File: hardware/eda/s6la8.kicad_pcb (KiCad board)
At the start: 4 copper layers, 100 x 64 mm, 155 parts, among them J1 2.54mm 6 x 1 THT Vertical Male, J2 2.54mm 2 x 1 THT Vertical Male, J3 2.54mm 10 x 2 THT Horizontal 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, J4 USB4105-GF-A, J5 2.54mm 3 x 1 THT Vertical Male, U1 24LC128-I/SN, U10 XC6SLX9-2TQG144C, U11 CY7C68013A-56PVXC, U12 TLV62569DBVR, U13 TLV62569DBVR, U14 MT48LC16M16A2P-6A, U2 USBLC6-2SC6, U3 USBLC6-2SC6, U4 USBLC6-2SC6, U5 USBLC6-2SC6, U6 USBLC6-2SC6, U7 SN74LVC245APWR, U8 SN74LVC8T245PWR, U9 SN74LVC2T45DCUR, Y1 ASE-50.000MHZ-LC-T, Y2 24MHz 12pF

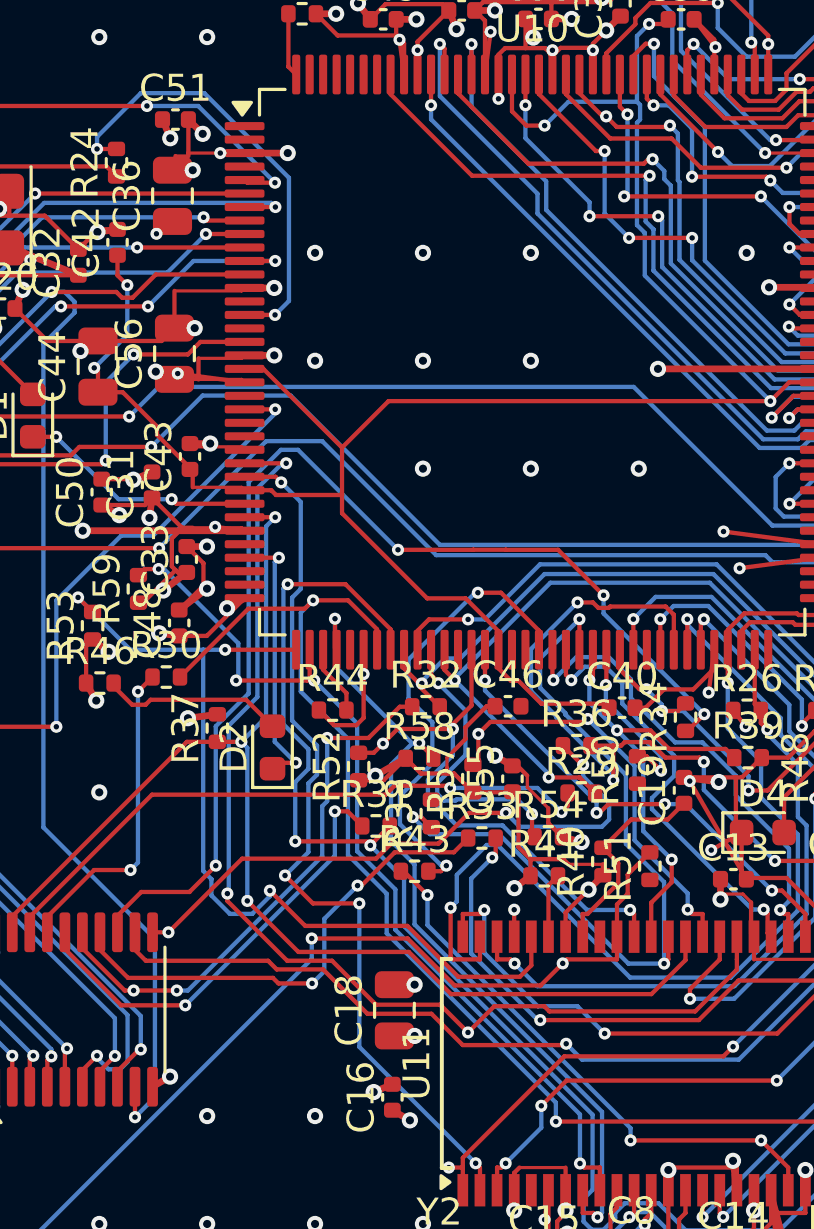
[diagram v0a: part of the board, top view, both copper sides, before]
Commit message: Add a grid router for leftover connections; 14 remain open
It closed INIT_B and two plane pads. The rest are FPGA bottom-row pads
enclosed by neighbouring escape routes and need tracks moved by hand.
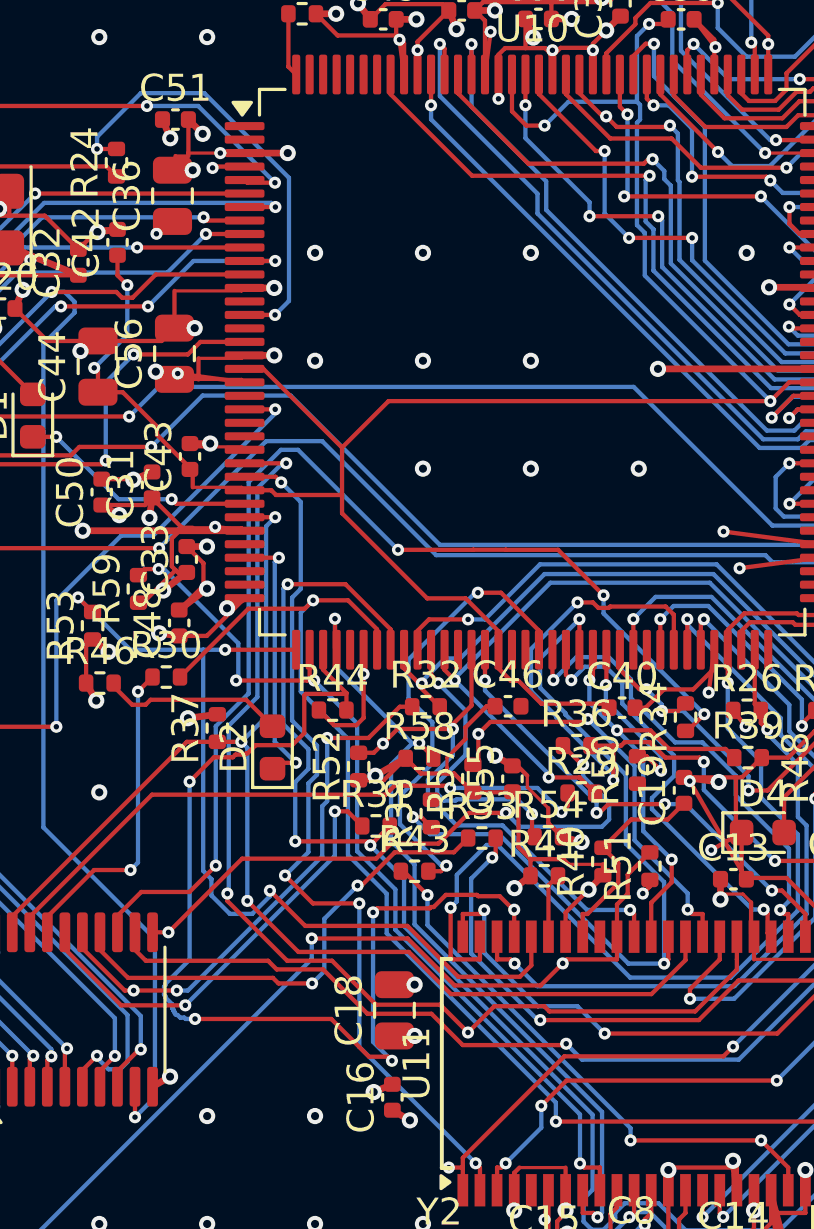
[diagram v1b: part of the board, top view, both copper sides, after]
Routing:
- net INIT_B: track 3.59 -> 41.0 mm, vias 1 -> 5
- net VCC_3V3: track 247.0 -> 248.9 mm, vias 81 -> 83

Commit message: Rip-up-and-reroute pass for leftover connections; 4 remain open
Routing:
- net FD1: track 47.7 -> 85.3 mm, vias 4 -> 5
- net GND: track 331.7 -> 358.1 mm, vias 295 -> 302
- net SLOE: track 15.6 -> 31.7 mm, vias 3 -> 7
- net SD_BA0: track 18.1 -> 32.2 mm
- net VCC_3V3: track 248.9 -> 259.3 mm, vias 83 -> 88
- net SD_DQ12: track 32.1 -> 37.7 mm, vias 5 -> 4
- net FD4: track 55.7 -> 54.5 mm
- net FLAGA: track 18.2 -> 18.9 mm

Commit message: Close all but one open connection; record ERC waiver
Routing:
- net MODE: track 35.3 -> 39.3 mm, vias 2 -> 1
- net GND: track 358.1 -> 359.8 mm, vias 302 -> 304
- net VCC_3V3: track 259.3 -> 260.5 mm, vias 88 -> 89
- net SLOE: track 31.7 -> 32.3 mm, vias 7 -> 6
- net FD7: track 30.6 -> 31.2 mm
- net REG_MOSI: track 34.0 -> 33.5 mm, vias 3 -> 2
- net TRIG: vias 3 -> 2
- net TCK: vias 1 -> 0
- net SD_DQ9: vias 7 -> 6
- net SD_DQ10: vias 3 -> 2
- net SD_CKE: vias 3 -> 2
- net SD_A9: vias 5 -> 4
- net SD_A8: vias 3 -> 2
- net SD_A6: vias 3 -> 2
- net SD_A5: vias 3 -> 2
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
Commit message: Route the last connection; add DNA board authentication and a printed case
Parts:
- moved C40 4.23 mm to (149.1, 98.8)
- moved C46 4.23 mm to (153.3, 98.8)
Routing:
- net VCC_3V3: track 260.5 -> 254.8 mm, vias 89 -> 91
- net VCC_1V2: track 123.3 -> 120.1 mm
